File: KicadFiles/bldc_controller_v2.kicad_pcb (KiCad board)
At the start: 4 copper layers, 51.5 x 89 mm, 172 parts, among them J1 Conn_01x05_Male, J10 Conn_01x02_Female, J11 Conn_01x02_Female, J12 Conn_01x02_Female, J13 Conn_01x02_Female, J14 Conn_01x02_Female, J15 Conn_01x04_Male, J2 Conn_01x03_Male, J3 Conn_01x03_Male, J4 1935174, J5 Conn_01x02_Female, J9 Conn_01x02_Female, Q10 IRLB8721PBF, Q11 IRLB8721PBF, Q2 DMN65D8L-7, Q3 DMN65D8L-7, Q5 IRF4905, Q6 IRLB8721PBF, Q7 IRLB8721PBF, Q8 IRLB8721PBF, Q9 IRLB8721PBF, SW2 D6C40 F1 LFS, SW3 1301.9314, SW4 1301.9314, SW5 SW_Push_DPDT, U1 ATmega328P-PU, U2 uA7810, U3 LM7805_TO220, U4 MCP601-xP, U5 LM339, U6 IRS2004, U7 IRS2004, U8 IRS2004, U9 HCPL-181-00DE, Y1 9B-16.000MBBK-B

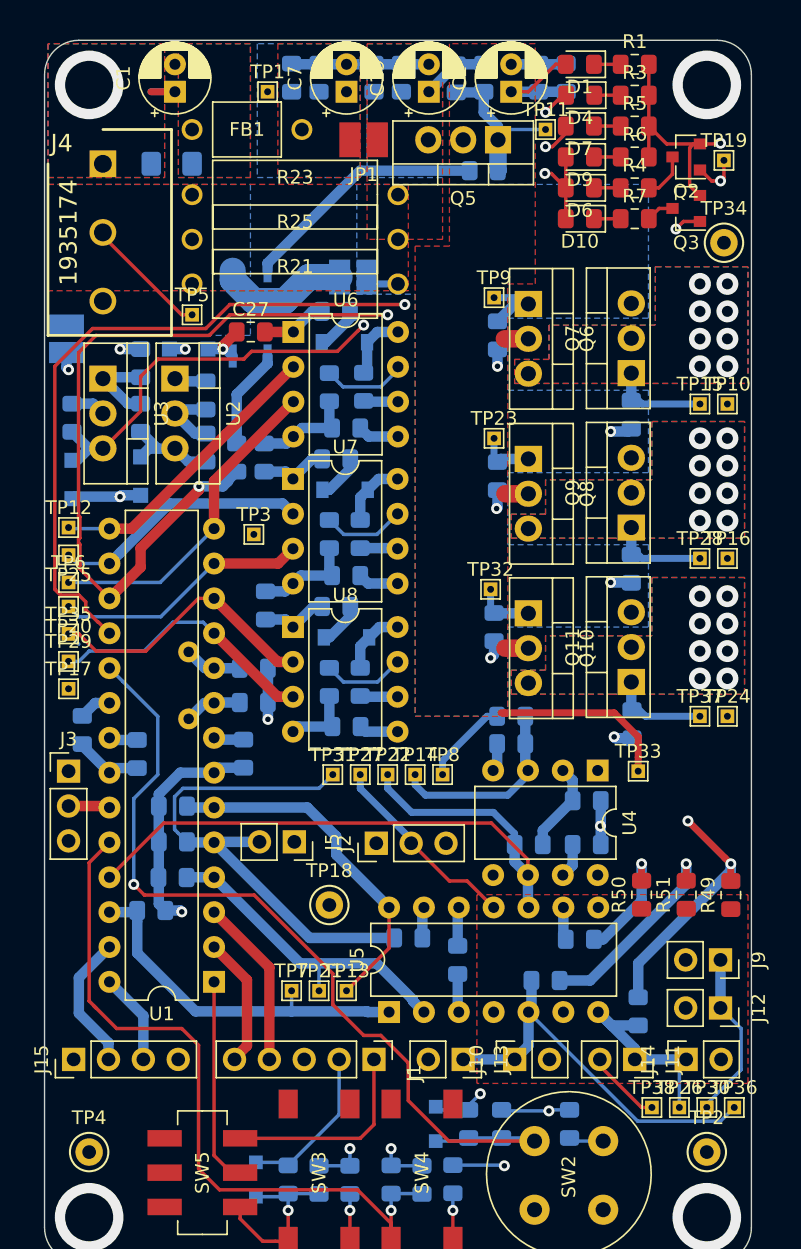
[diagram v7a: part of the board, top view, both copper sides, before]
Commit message: Started Fixing Top Silk
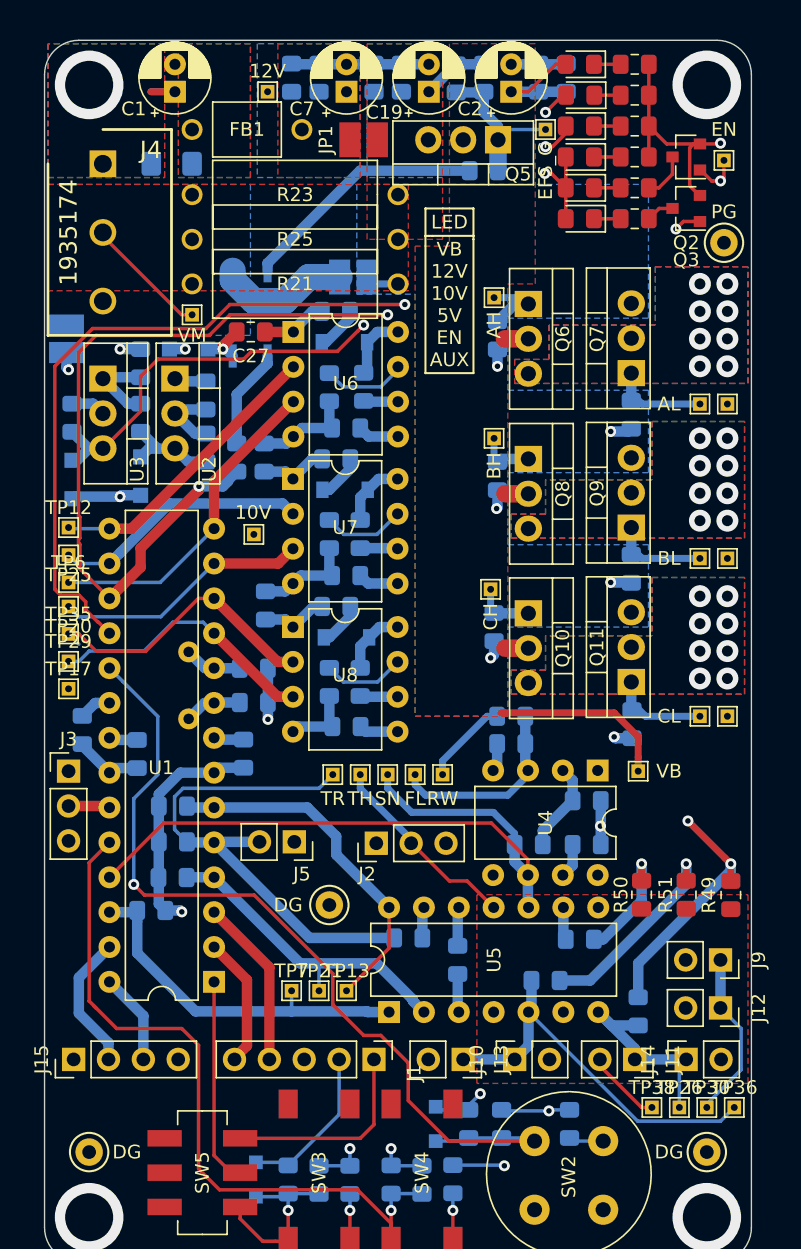
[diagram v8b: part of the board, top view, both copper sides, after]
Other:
- board text added: "10V"
- board text added: "12V"
- board text added: "AH"
- board text added: "AL"
- board text added: "BH"
- board text added: "BL"
- board text added: "CH"
- board text added: "CL"
- board text added: "DG"
- board text added: "EFS_G"
- board text added: "EN"
- board text added: "FL"
- board text added: "LED"
- board text added: "PG"
- board text added: "RW"
- board text added: "SN"
- board text added: "TH"
- board text added: "TR"
- board text added: "VB"
- board text added: "VB 12V 10V 5V EN AUX"
- board text added: "VM"
